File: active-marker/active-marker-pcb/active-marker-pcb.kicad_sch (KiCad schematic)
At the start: 44 parts, among them J1 Conn_01x10, J13 Conn_01x04, J2 Conn_01x04, J3 Conn_01x04, J4 Conn_01x04, J5 Conn_01x04, J6 Conn_01x04, J7 Conn_01x04, SW1 SW_DIP_x02, SW2 SW_Push, SW3 SW_Push, SW4 SW_Push, U1 220ADA16, U2 XC6206PxxxMR, U3 VEML6030, U4 VEML6030, U5 MCP2551-I-P, U6 STM32F303K8Tx, Y1 NX3225GA-32M

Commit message: fix Pinmap and add some vias
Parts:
- added H1, H2, H3: MountingHole, MountingHole:MountingHole_3.2mm_M3_ISO7380, symbol Mechanical:MountingHole
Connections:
- net CAN+: now also J13.2 (Pin_2); no longer J13.1 (Pin_1)
- net CAN-: now also J13.1 (Pin_1); no longer J13.2 (Pin_2)
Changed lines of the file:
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@@
     (effects (font (size 1.27 1.27)) (justify left bottom))
   )
-  (label "CAN+" (at 142.875 167.64 180)
+  (label "CAN+" (at 142.875 170.18 180)
     (effects (font (size 1.27 1.27)) (justify right bottom))
   )
@@
     (effects (font (size 1.27 1.27)) (justify right bottom))
   )
-  (label "CAN-" (at 142.875 170.18 180)
+  (label "CAN-" (at 142.875 167.64 180)
     (effects (font (size 1.27 1.27)) (justify right bottom))
   )
@@
     (pin "7")
     (pin "8")
+  )
+  (symbol (lib_id "Mechanical:MountingHole") (at 76.2 177.8 0) (unit 1)
+    (in_bom yes) (on_board yes) (fields_autoplaced)
+    (property "Reference" "H1" (id 0) (at 78.74 176.9653 0)
+      (effects (font (size 1.27 1.27)) (justify left))
+    )
+    (property "Value" "MountingHole" (id 1) (at 78.74 179.5022 0)
+      (effects (font (size 1.27 1.27)) (justify left))
+    )
+    (property "Footprint" "MountingHole:MountingHole_3.2mm_M3_ISO7380" (id 2) (at 76.2 177.8 0)
+      (effects (font (size 1.27 1.27)) hide)
+    )
+    (property "Datasheet" "~" (id 3) (at 76.2 177.8 0)
+      (effects (font (size 1.27 1.27)) hide)
+    )
   )
   (symbol (lib_id "power:GND") (at 31.75 88.9 0) (unit 1)
@@
     (pin "1")
   )
+  (symbol (lib_id "Mechanical:MountingHole") (at 76.2 184.15 0) (unit 1)
+    (in_bom yes) (on_board yes) (fields_autoplaced)
+    (property "Reference" "H2" (id 0) (at 78.74 183.3153 0)
+      (effects (font (size 1.27 1.27)) (justify left))
+    )
+    (property "Value" "MountingHole" (id 1) (at 78.74 185.8522 0)
+      (effects (font (size 1.27 1.27)) (justify left))
+    )
+    (property "Footprint" "MountingHole:MountingHole_3.2mm_M3_ISO7380" (id 2) (at 76.2 184.15 0)
+      (effects (font (size 1.27 1.27)) hide)
+    )
+    (property "Datasheet" "~" (id 3) (at 76.2 184.15 0)
+      (effects (font (size 1.27 1.27)) hide)
+    )
+  )
   (symbol (lib_id "Device:R_Pack04_SIP_Split") (at 29.845 106.045 180) (unit 3)
     (in_bom yes) (on_board yes)
@@
     )
     (pin "1")
+  )
+  (symbol (lib_id "Mechanical:MountingHole") (at 76.2 190.5 0) (unit 1)
+    (in_bom yes) (on_board yes) (fields_autoplaced)
+    (property "Reference" "H3" (id 0) (at 78.74 189.6653 0)
+      (effects (font (size 1.27 1.27)) (justify left))
+    )
+    (property "Value" "MountingHole" (id 1) (at 78.74 192.2022 0)
+      (effects (font (size 1.27 1.27)) (justify left))
+    )
+    (property "Footprint" "MountingHole:MountingHole_3.2mm_M3_ISO7380" (id 2) (at 76.2 190.5 0)
+      (effects (font (size 1.27 1.27)) hide)
+    )
+    (property "Datasheet" "~" (id 3) (at 76.2 190.5 0)
+      (effects (font (size 1.27 1.27)) hide)
+    )
   )
   (symbol (lib_id "power:+3V3") (at 89.535 62.23 0) (unit 1)
@@
       (reference "D2") (unit 1) (value "LED_Small") (footprint "LED_SMD:LED_0603_1608Metric_Pad1.05x0.95mm_HandSolder")
     )
+    (path "/0f87c1a0-5c4e-45d1-aa9c-634f5d5a72be"
+      (reference "H1") (unit 1) (value "MountingHole") (footprint "MountingHole:MountingHole_3.2mm_M3_ISO7380")
+    )
+    (path "/695103a4-f9e9-4a52-8dfd-792d01738a0c"
+      (reference "H2") (unit 1) (value "MountingHole") (footprint "MountingHole:MountingHole_3.2mm_M3_ISO7380")
+    )
+    (path "/8da03cec-58c6-4654-96f8-6b08c056b501"
+      (reference "H3") (unit 1) (value "MountingHole") (footprint "MountingHole:MountingHole_3.2mm_M3_ISO7380")
+    )
     (path "/4b5523ff-6219-41da-b842-f948ddf68bd2"

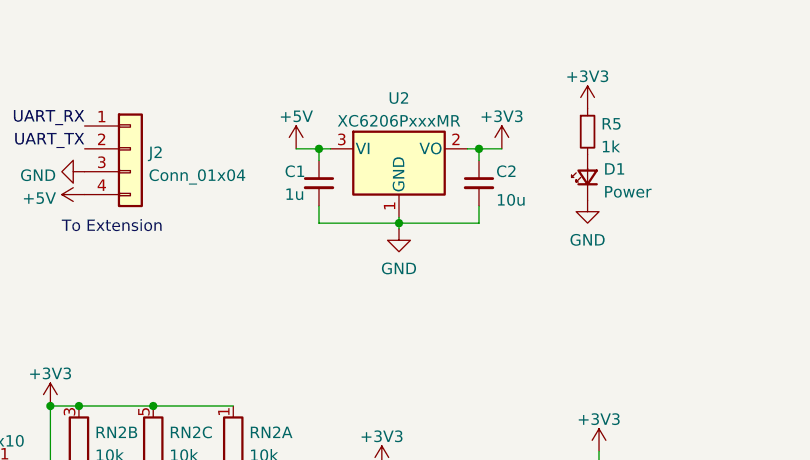
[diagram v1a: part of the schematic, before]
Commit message: add diode, fix gerber files
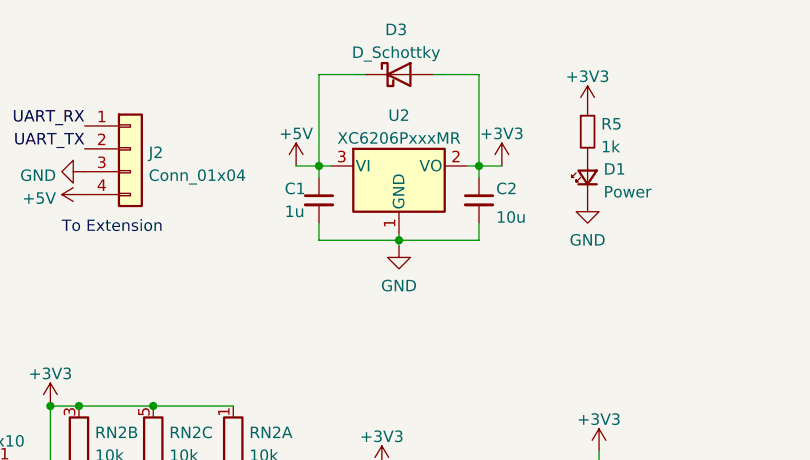
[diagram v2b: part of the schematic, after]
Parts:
- added D3: D_Schottky, Diode_SMD:D_SOD-523, symbol Device:D_Schottky
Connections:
- net +3V3: now also D3.2 (A)
- net +5V: now also D3.1 (K)
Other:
- moved on the sheet: C1, C2, U2

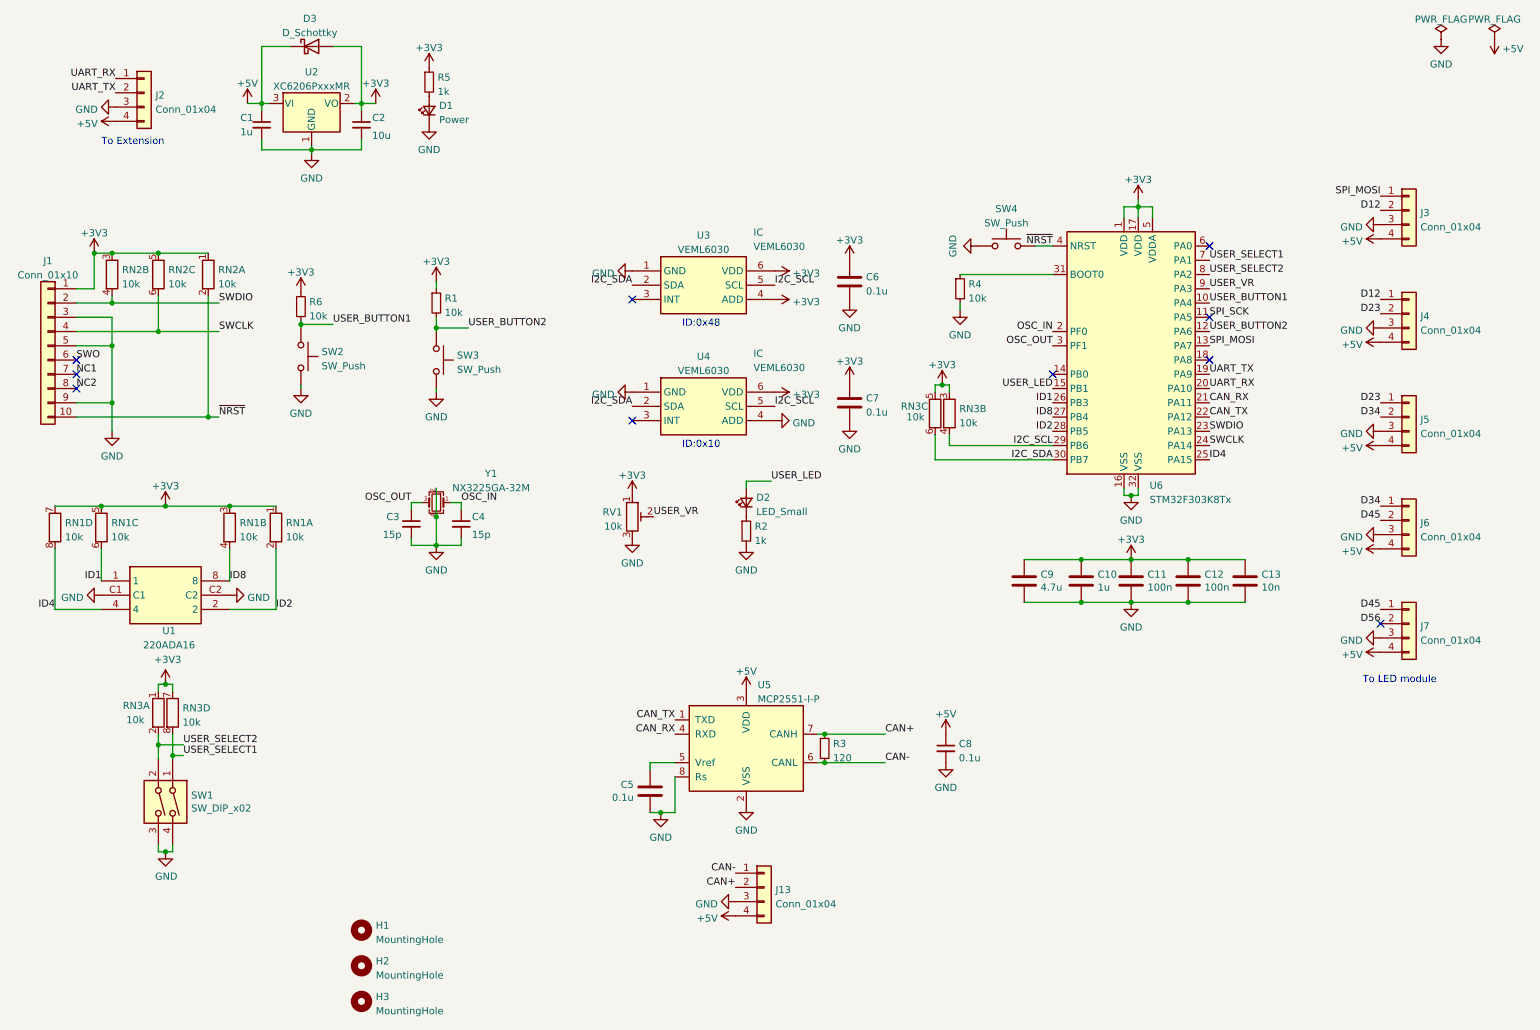
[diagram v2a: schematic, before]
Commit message: delete can and so on
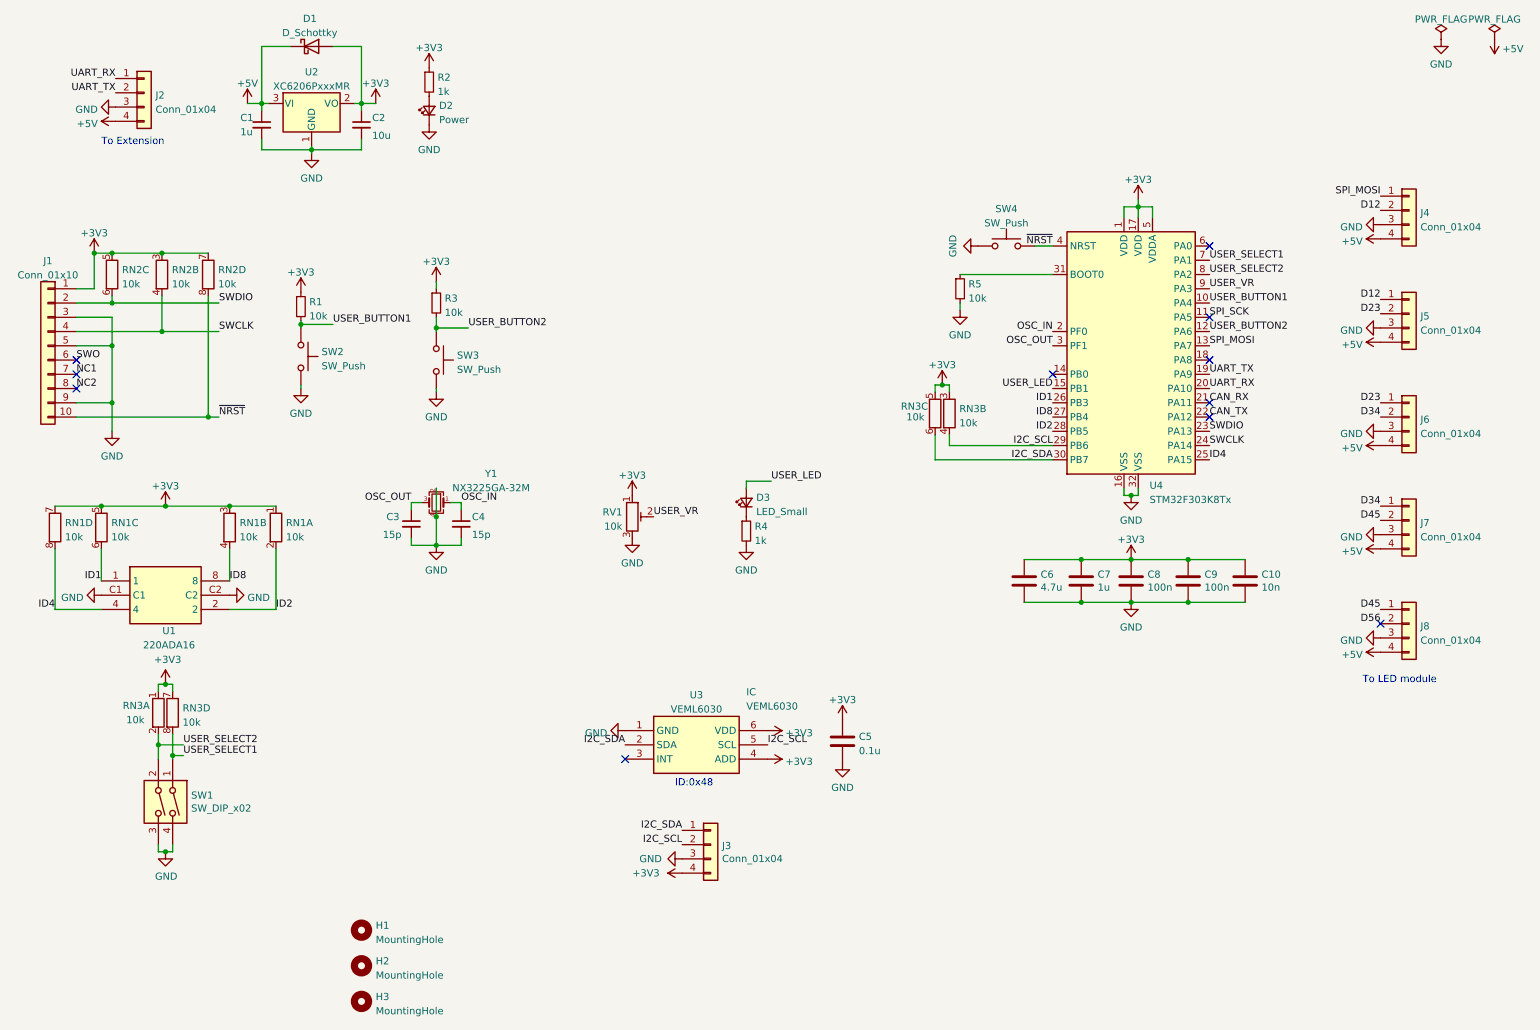
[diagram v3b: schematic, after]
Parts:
- removed C5, C7: 0.1u, Capacitor_SMD:C_0603_1608Metric_Pad1.08x0.95mm_HandSolder, symbol Device:C
- removed C8: 0.1u, Capacitor_SMD:C_0603_1608Metric_Pad1.08x0.95mm_HandSolder, symbol Device:C_Small
- removed J13: Conn_01x04, active-marker:JST_S4B-ZR_LF__SN_, symbol Connector_Generic:Conn_01x04
- removed R3: 120, Resistor_SMD:R_0603_1608Metric_Pad0.98x0.95mm_HandSolder, symbol Device:R_Small
- removed U4: VEML6030, active-marker:VEML6030, symbol active-marker:VEML6030
- removed U5: MCP2551-I-P, Package_SO:SOIC-8_3.9x4.9mm_P1.27mm, symbol Interface_CAN_LIN:MCP2551-I-P
- added J3: Conn_01x04, active-marker:JST_S4B-ZR_LF__SN_, symbol Connector_Generic:Conn_01x04
- renumbered C13 to C10, C6 to C5, C9 to C6, C10 to C7, C11 to C8, C12 to C9, D3 to D1, D1 to D2, D2 to D3, J3 to J4, J4 to J5, J5 to J6, J6 to J7, J7 to J8, R6 to R1, R5 to R2, R1 to R3, R2 to R4, R4 to R5, U6 to U4
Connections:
- net +3V3: now also RN2.7 (R4.1), J3.4 (Pin_4); no longer RN2.1 (R1.1)
- net GND: now also J3.3 (Pin_3)
- net I2C_SCL: now also J3.2 (Pin_2)
- net I2C_SDA: now also J3.1 (Pin_1)
- net SWCLK: now also RN2.4 (R2.2); no longer RN2.6 (R3.2)
- net SWDIO: now also RN2.6 (R3.2); no longer RN2.4 (R2.2)
- net ~{NRST}: now also RN2.8 (R4.2); no longer RN2.2 (R1.2)
- no-connect marks 10 -> 11
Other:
- note removed: "ID:0x10"
- moved on the sheet: C5, RN2B, RN2C, U3
